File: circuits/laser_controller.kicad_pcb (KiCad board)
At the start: 4 copper layers, 173 x 61.1 mm, 180 parts, among them J1 USB_MINI_B, J2 USB_MINI_B, J5 24V DC IN, J6 CONN_RJ45, Q1 SOT-23, Q2 SOT-23, Q3 SOT-23, Q4 SOT-23, Q5 SOT-23, Q6 SOT-23, SW1 SW_PUSH, SW2 SW_PUSH, SW3 SW_PUSH, U1 SOIC-8_3.9x4.9mm_P1.27mm, U10 QFN-28-1EP_5x5mm_P0.5mm_EP3.3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, U11 SOT-23-5, U12 TSSOP-14_4.4x5mm_P0.65mm, U13 SOT-23, U14 LQFP-64_10x10mm_P0.5mm, U15 TSOT-23-6, U16 TSOT-23-6, U2 SOIC-8_3.9x4.9mm_P1.27mm, U3 SOIC-8_3.9x4.9mm_P1.27mm, U4 SOIC-8_3.9x4.9mm_P1.27mm, U5 SOT-23-5, U6 SOT-23-5, U7 SOT-23-5, U8 SOT-23-5, U9 ESP32-S3-WROOM-1

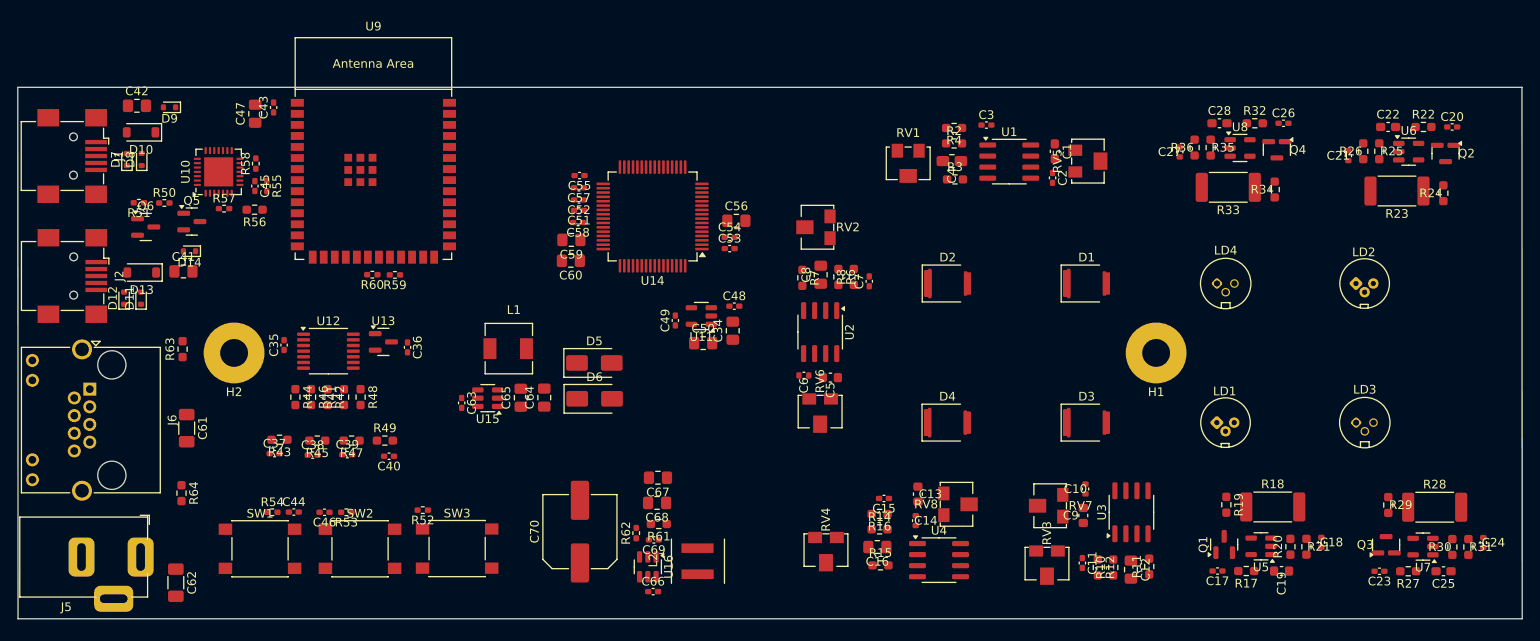
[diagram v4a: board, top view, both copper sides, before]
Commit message: Fix: revert to known-good, add GND vias at JLCPCB min (0.6/0.3), presets in pro file only
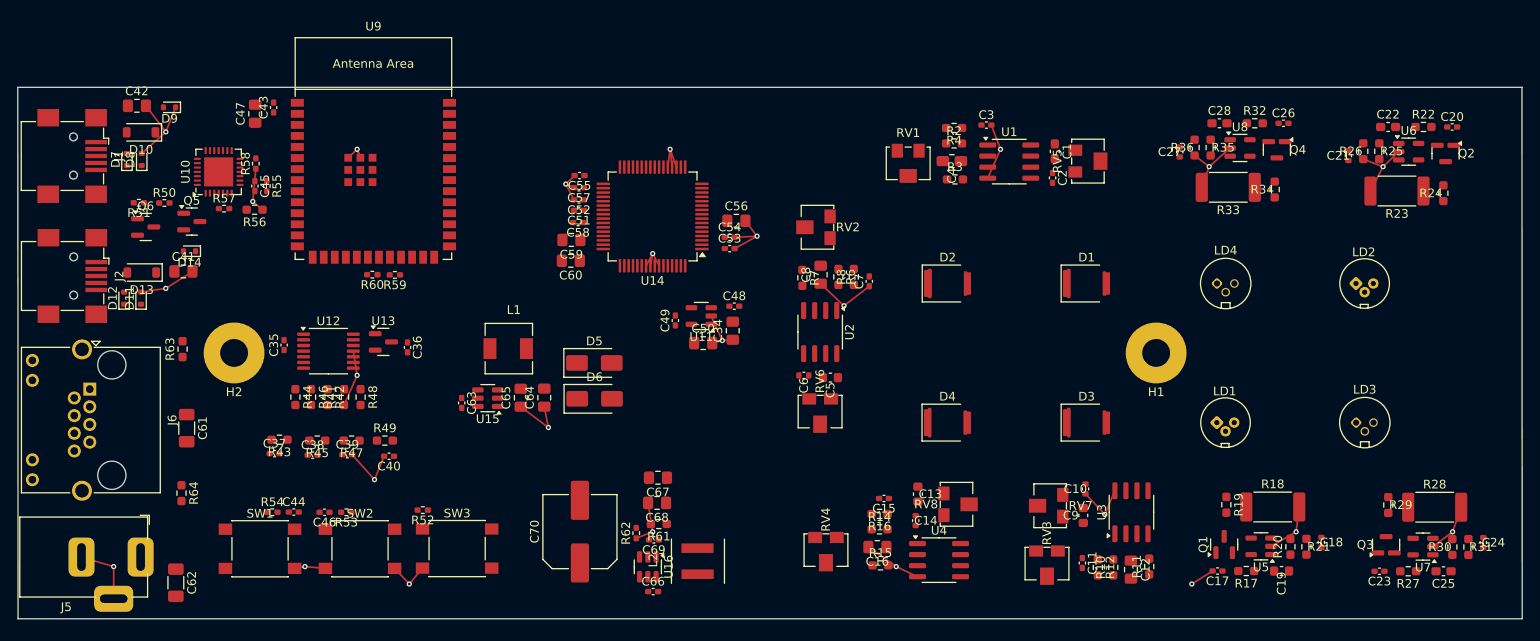
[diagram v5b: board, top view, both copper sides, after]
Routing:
- net GND: track 0.00 -> 153.2 mm, vias 0 -> 25
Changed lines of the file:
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@@
     (effects (font (size 1.2 1.2) (thickness 0.18)))
   )
+  (segment (start 103.7325 100.4000) (end 104.0000 99.0000) (width 0.2) (layer "F.Cu") (net 46))
+  (segment (start 104.7325 100.4000) (end 104.0000 99.0000) (width 0.2) (layer "F.Cu") (net 46))
+  (segment (start 103.2325 100.4000) (end 104.0000 99.0000) (width 0.2) (layer "F.Cu") (net 46))
+  (segment (start 70.3750 87.9750) (end 70.0000 87.0000) (width 0.2) (layer "F.Cu") (net 46))
+  (segment (start 70.3750 87.9750) (end 70.0000 87.0000) (width 0.2) (layer "F.Cu") (net 46))
+  (segment (start 68.9750 87.9750) (end 70.0000 87.0000) (width 0.2) (layer "F.Cu") (net 46))
+  (segment (start 106.2325 89.0500) (end 106.0000 87.0000) (width 0.2) (layer "F.Cu") (net 46))
+  (segment (start 105.7325 89.0500) (end 106.0000 87.0000) (width 0.2) (layer "F.Cu") (net 46))
+  (segment (start 106.7325 89.0500) (end 106.0000 87.0000) (width 0.2) (layer "F.Cu") (net 46))
+  (segment (start 166.3240 87.7155) (end 168.0000 89.0000) (width 0.2) (layer "F.Cu") (net 46))
+  (segment (start 167.1500 91.3750) (end 168.0000 89.0000) (width 0.2) (layer "F.Cu") (net 46))
+  (segment (start 170.4085 86.8490) (end 168.0000 89.0000) (width 0.2) (layer "F.Cu") (net 46))
+  (segment (start 94.9475 91.4250) (end 94.0000 91.0000) (width 0.2) (layer "F.Cu") (net 46))
+  (segment (start 95.0150 90.0250) (end 94.0000 91.0000) (width 0.2) (layer "F.Cu") (net 46))
+  (segment (start 94.9475 92.8250) (end 94.0000 91.0000) (width 0.2) (layer "F.Cu") (net 46))
+  (segment (start 185.7240 88.1405) (end 188.0000 89.0000) (width 0.2) (layer "F.Cu") (net 46))
+  (segment (start 189.8085 87.2740) (end 188.0000 89.0000) (width 0.2) (layer "F.Cu") (net 46))
+  (segment (start 186.5500 91.8000) (end 188.0000 89.0000) (width 0.2) (layer "F.Cu") (net 46))
+  (segment (start 114.6575 95.2250) (end 116.0000 97.0000) (width 0.2) (layer "F.Cu") (net 46))
+  (segment (start 113.4175 97.1250) (end 116.0000 97.0000) (width 0.2) (layer "F.Cu") (net 46))
+  (segment (start 113.4175 98.4250) (end 116.0000 97.0000) (width 0.2) (layer "F.Cu") (net 46))
+  (segment (start 110.8400 109.2950) (end 112.0000 109.0000) (width 0.2) (layer "F.Cu") (net 46))
+  (segment (start 113.2025 108.9075) (end 112.0000 109.0000) (width 0.2) (layer "F.Cu") (net 46))
+  (segment (start 110.7275 106.1750) (end 112.0000 109.0000) (width 0.2) (layer "F.Cu") (net 46))
+  (segment (start 49.1250 82.1750) (end 48.0000 85.0000) (width 0.2) (layer "F.Cu") (net 46))
+  (segment (start 45.2250 87.4750) (end 48.0000 85.0000) (width 0.2) (layer "F.Cu") (net 46))
+  (segment (start 45.7125 82.0000) (end 48.0000 85.0000) (width 0.2) (layer "F.Cu") (net 46))
+  (segment (start 193.7295 132.6955) (end 196.0000 131.0000) (width 0.2) (layer "F.Cu") (net 46))
+  (segment (start 196.9880 128.1695) (end 196.0000 131.0000) (width 0.2) (layer "F.Cu") (net 46))
+  (segment (start 178.3610 128.1415) (end 178.0000 131.0000) (width 0.2) (layer "F.Cu") (net 46))
+  (segment (start 175.1025 132.6675) (end 178.0000 131.0000) (width 0.2) (layer "F.Cu") (net 46))
+  (segment (start 157.1550 126.2750) (end 156.0000 129.0000) (width 0.2) (layer "F.Cu") (net 46))
+  (segment (start 153.7755 126.6350) (end 156.0000 129.0000) (width 0.2) (layer "F.Cu") (net 46))
+  (segment (start 142.9480 84.2160) (end 144.0000 87.0000) (width 0.2) (layer "F.Cu") (net 46))
+  (segment (start 142.5310 90.3225) (end 144.0000 87.0000) (width 0.2) (layer "F.Cu") (net 46))
+  (segment (start 134.4500 136.1600) (end 132.0000 135.0000) (width 0.2) (layer "F.Cu") (net 46))
+  (segment (start 128.8000 132.7500) (end 132.0000 135.0000) (width 0.2) (layer "F.Cu") (net 46))
+  (segment (start 128.9055 102.7570) (end 126.0000 105.0000) (width 0.2) (layer "F.Cu") (net 46))
+  (segment (start 123.3175 102.4650) (end 126.0000 105.0000) (width 0.2) (layer "F.Cu") (net 46))
+  (segment (start 102.1000 131.7450) (end 104.0000 131.0000) (width 0.2) (layer "F.Cu") (net 46))
+  (segment (start 103.4625 127.6750) (end 104.0000 131.0000) (width 0.2) (layer "F.Cu") (net 46))
+  (segment (start 91.5250 116.6000) (end 92.0000 119.0000) (width 0.2) (layer "F.Cu") (net 46))
+  (segment (start 88.8250 116.6125) (end 92.0000 119.0000) (width 0.2) (layer "F.Cu") (net 46))
+  (segment (start 77.5225 135.1750) (end 76.0000 137.0000) (width 0.2) (layer "F.Cu") (net 46))
+  (segment (start 74.3125 135.2000) (end 76.0000 137.0000) (width 0.2) (layer "F.Cu") (net 46))
+  (segment (start 73.1050 122.3050) (end 72.0000 125.0000) (width 0.2) (layer "F.Cu") (net 46))
+  (segment (start 69.4400 122.1300) (end 72.0000 125.0000) (width 0.2) (layer "F.Cu") (net 46))
+  (segment (start 69.5625 110.2175) (end 70.0000 113.0000) (width 0.2) (layer "F.Cu") (net 46))
+  (segment (start 68.5000 116.4175) (end 70.0000 113.0000) (width 0.2) (layer "F.Cu") (net 46))
+  (segment (start 62.8125 135.2000) (end 64.0000 135.0000) (width 0.2) (layer "F.Cu") (net 46))
+  (segment (start 66.3525 135.2000) (end 64.0000 135.0000) (width 0.2) (layer "F.Cu") (net 46))
+  (segment (start 59.1225 93.9500) (end 58.0000 93.0000) (width 0.2) (layer "F.Cu") (net 46))
+  (segment (start 58.3500 89.2450) (end 58.0000 93.0000) (width 0.2) (layer "F.Cu") (net 46))
+  (segment (start 45.1500 103.4250) (end 48.0000 103.0000) (width 0.2) (layer "F.Cu") (net 46))
+  (segment (start 51.0625 101.0500) (end 48.0000 103.0000) (width 0.2) (layer "F.Cu") (net 46))
+  (segment (start 42.0000 138.7000) (end 42.0000 135.0000) (width 0.2) (layer "F.Cu") (net 46))
+  (segment (start 38.3000 133.9000) (end 42.0000 135.0000) (width 0.2) (layer "F.Cu") (net 46))
+  (segment (start 168.3935 135.5075) (end 166.0000 137.0000) (width 0.2) (layer "F.Cu") (net 46))
+  (via (at 104 99) (size 0.6) (drill 0.3) (layers "F.Cu" "B.Cu") (net 46))
+  (via (at 70 87) (size 0.6) (drill 0.3) (layers "F.Cu" "B.Cu") (net 46))
+  (via (at 106 87) (size 0.6) (drill 0.3) (layers "F.Cu" "B.Cu") (net 46))
+  (via (at 168 89) (size 0.6) (drill 0.3) (layers "F.Cu" "B.Cu") (net 46))
+  (via (at 94 91) (size 0.6) (drill 0.3) (layers "F.Cu" "B.Cu") (net 46))
+  (via (at 188 89) (size 0.6) (drill 0.3) (layers "F.Cu" "B.Cu") (net 46))
+  (via (at 116 97) (size 0.6) (drill 0.3) (layers "F.Cu" "B.Cu") (net 46))
+  (via (at 112 109) (size 0.6) (drill 0.3) (layers "F.Cu" "B.Cu") (net 46))
+  (via (at 48 85) (size 0.6) (drill 0.3) (layers "F.Cu" "B.Cu") (net 46))
+  (via (at 196 131) (size 0.6) (drill 0.3) (layers "F.Cu" "B.Cu") (net 46))
+  (via (at 178 131) (size 0.6) (drill 0.3) (layers "F.Cu" "B.Cu") (net 46))
+  (via (at 156 129) (size 0.6) (drill 0.3) (layers "F.Cu" "B.Cu") (net 46))
+  (via (at 144 87) (size 0.6) (drill 0.3) (layers "F.Cu" "B.Cu") (net 46))
+  (via (at 132 135) (size 0.6) (drill 0.3) (layers "F.Cu" "B.Cu") (net 46))
+  (via (at 126 105) (size 0.6) (drill 0.3) (layers "F.Cu" "B.Cu") (net 46))
+  (via (at 104 131) (size 0.6) (drill 0.3) (layers "F.Cu" "B.Cu") (net 46))
+  (via (at 92 119) (size 0.6) (drill 0.3) (layers "F.Cu" "B.Cu") (net 46))
+  (via (at 76 137) (size 0.6) (drill 0.3) (layers "F.Cu" "B.Cu") (net 46))
+  (via (at 72 125) (size 0.6) (drill 0.3) (layers "F.Cu" "B.Cu") (net 46))
+  (via (at 70 113) (size 0.6) (drill 0.3) (layers "F.Cu" "B.Cu") (net 46))
+  (via (at 64 135) (size 0.6) (drill 0.3) (layers "F.Cu" "B.Cu") (net 46))
+  (via (at 58 93) (size 0.6) (drill 0.3) (layers "F.Cu" "B.Cu") (net 46))
+  (via (at 48 103) (size 0.6) (drill 0.3) (layers "F.Cu" "B.Cu") (net 46))
+  (via (at 42 135) (size 0.6) (drill 0.3) (layers "F.Cu" "B.Cu") (net 46))
+  (via (at 166 137) (size 0.6) (drill 0.3) (layers "F.Cu" "B.Cu") (net 46))
   (zone (net 46) (net_name "GND") (layer "In1.Cu") (hatch edge 0.508)
     (connect_pads (clearance 0.508))

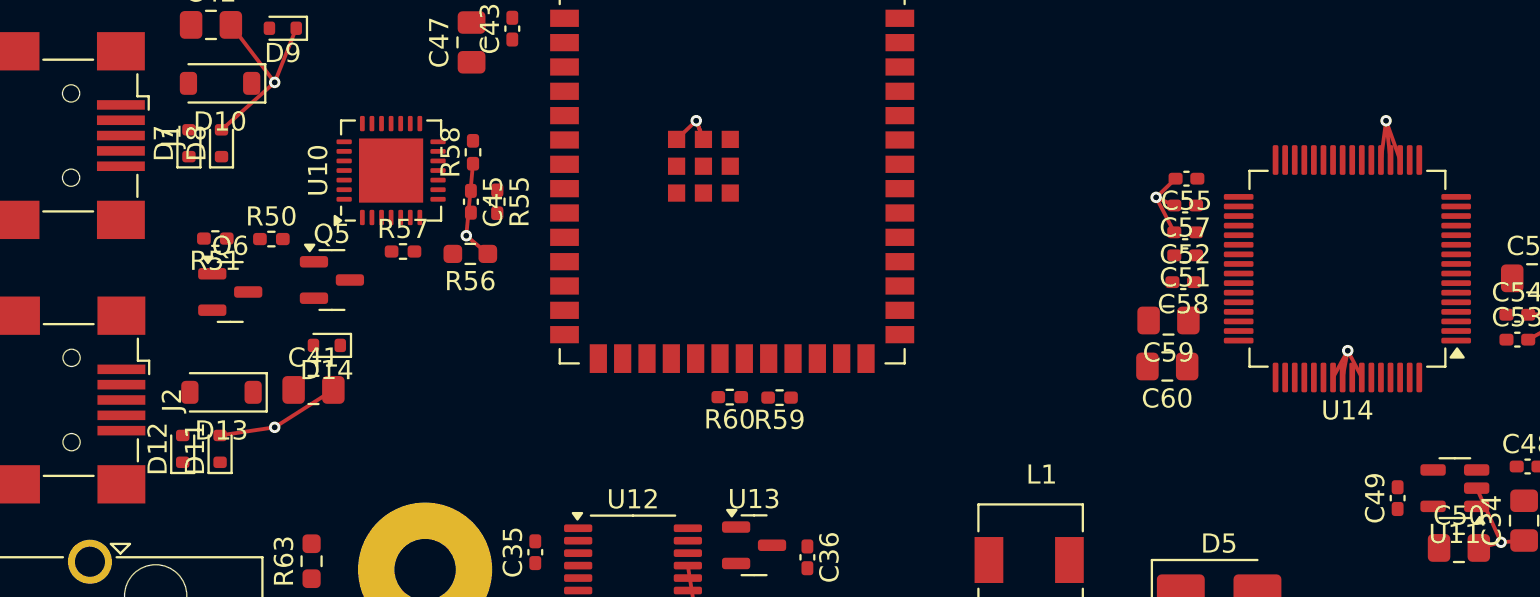
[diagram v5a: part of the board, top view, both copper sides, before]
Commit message: Fix D11/J6 pad overlap — move D11 from (45.15,104.13) to (42,104)
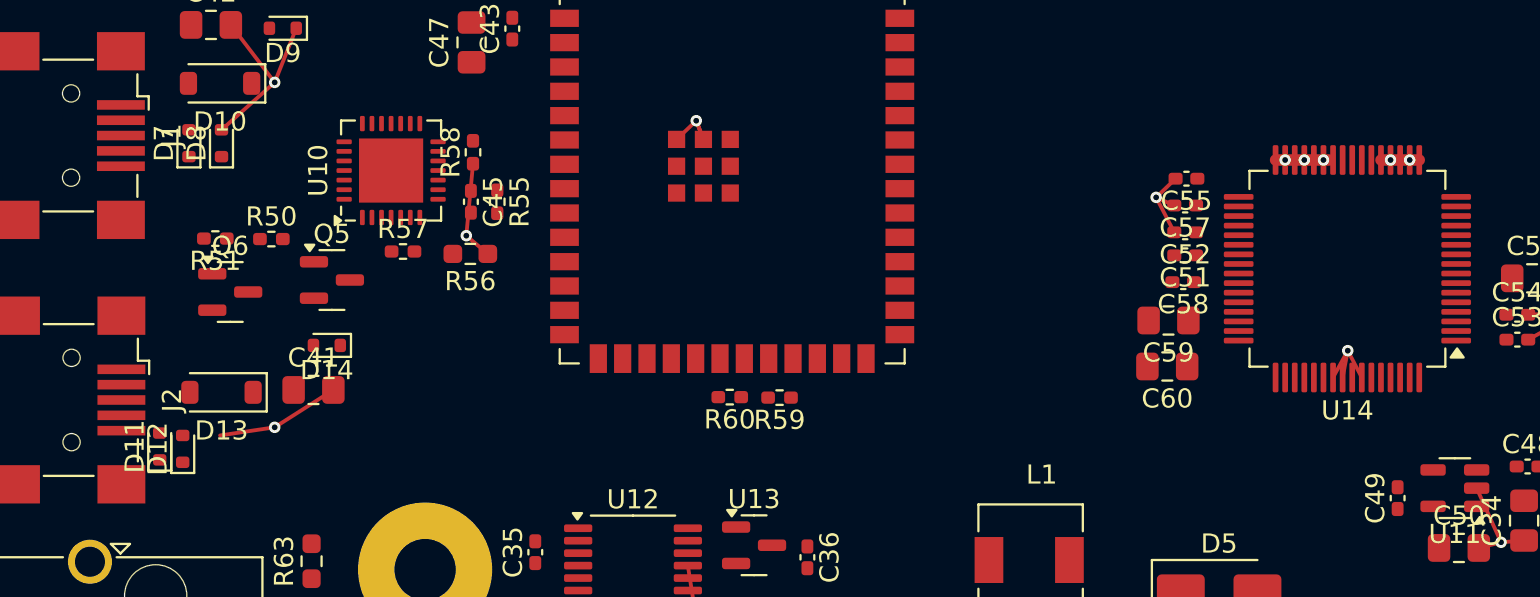
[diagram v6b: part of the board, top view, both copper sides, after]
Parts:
- moved D11 3.15 mm to (42.0, 104.0)
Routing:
- net GND: track 153.2 -> 139.1 mm, vias 25 -> 27
- net /POWER_IO/BUCK_5V: track 0.00 -> 6.42 mm, vias 0 -> 1
- net +5V: track 0.00 -> 6.21 mm, vias 0 -> 1
